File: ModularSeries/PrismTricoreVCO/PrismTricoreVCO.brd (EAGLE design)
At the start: 81 x 49 mm, 56 parts, among them IC1 LM13700_DIP, IC2 TL0X4_DIP, IC3 TL0X4_DIP, Q1 2N3906, Q2 2N3906

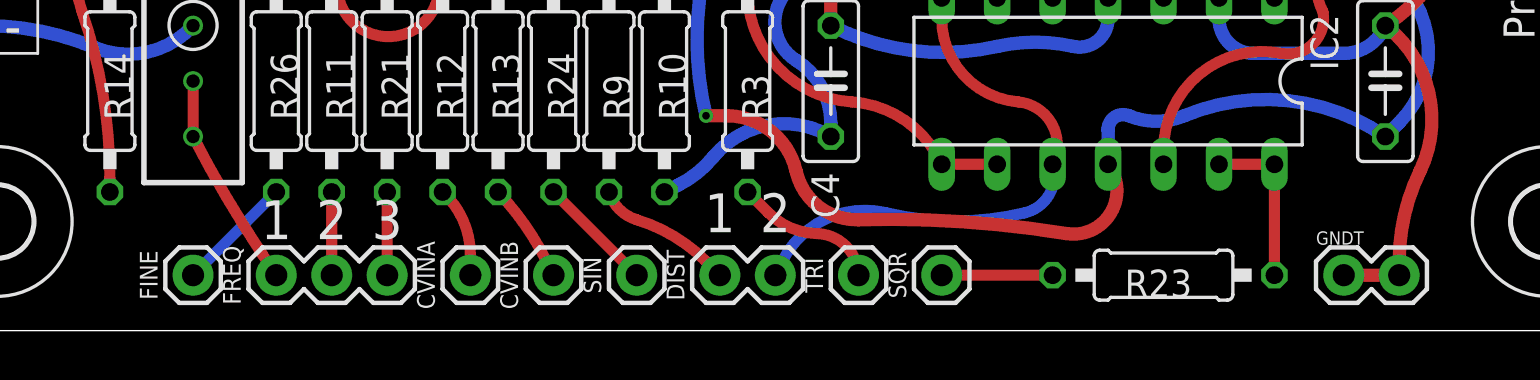
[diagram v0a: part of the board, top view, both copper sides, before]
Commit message: Updates to Prism, VCA, PSU and Prism BOM added
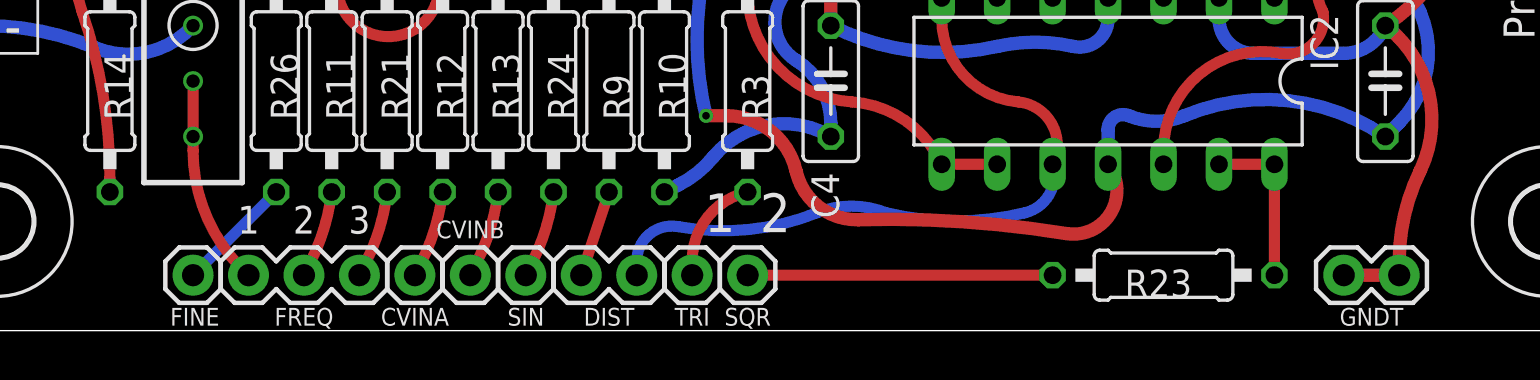
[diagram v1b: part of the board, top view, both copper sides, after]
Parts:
- moved SQR 8.89 mm to (39.4, 2.54)
- moved TRI 7.62 mm to (36.8, 2.54)
- moved DIST 6.35 mm to (31.8, 2.54)
- moved SIN 5.08 mm to (29.2, 2.54)
- moved CVINB 3.81 mm to (26.7, 2.54)
- moved CVINA 2.54 mm to (24.1, 2.54)
- moved FREQ 1.27 mm to (16.5, 2.54)
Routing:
- net N$30: track 5.08 -> 14.0 mm
- net N$2: track 54.5 -> 61.2 mm
- net N$13: track 6.40 -> 4.02 mm
- net N$29: track 6.46 -> 4.70 mm
- net N$31: track 5.39 -> 4.02 mm
- net N$28: track 4.59 -> 4.02 mm
- net N$25: track 9.95 -> 9.43 mm

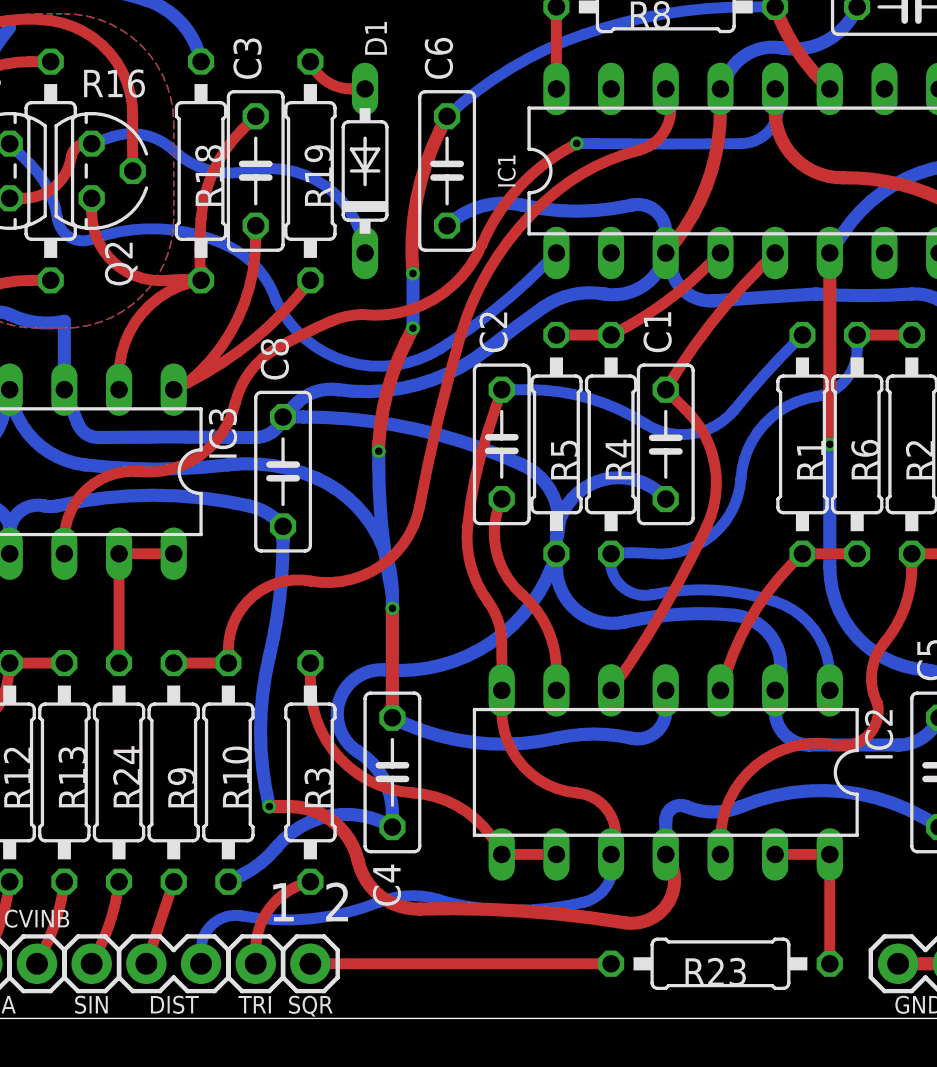
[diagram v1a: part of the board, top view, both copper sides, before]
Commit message: C2 removed from Prism
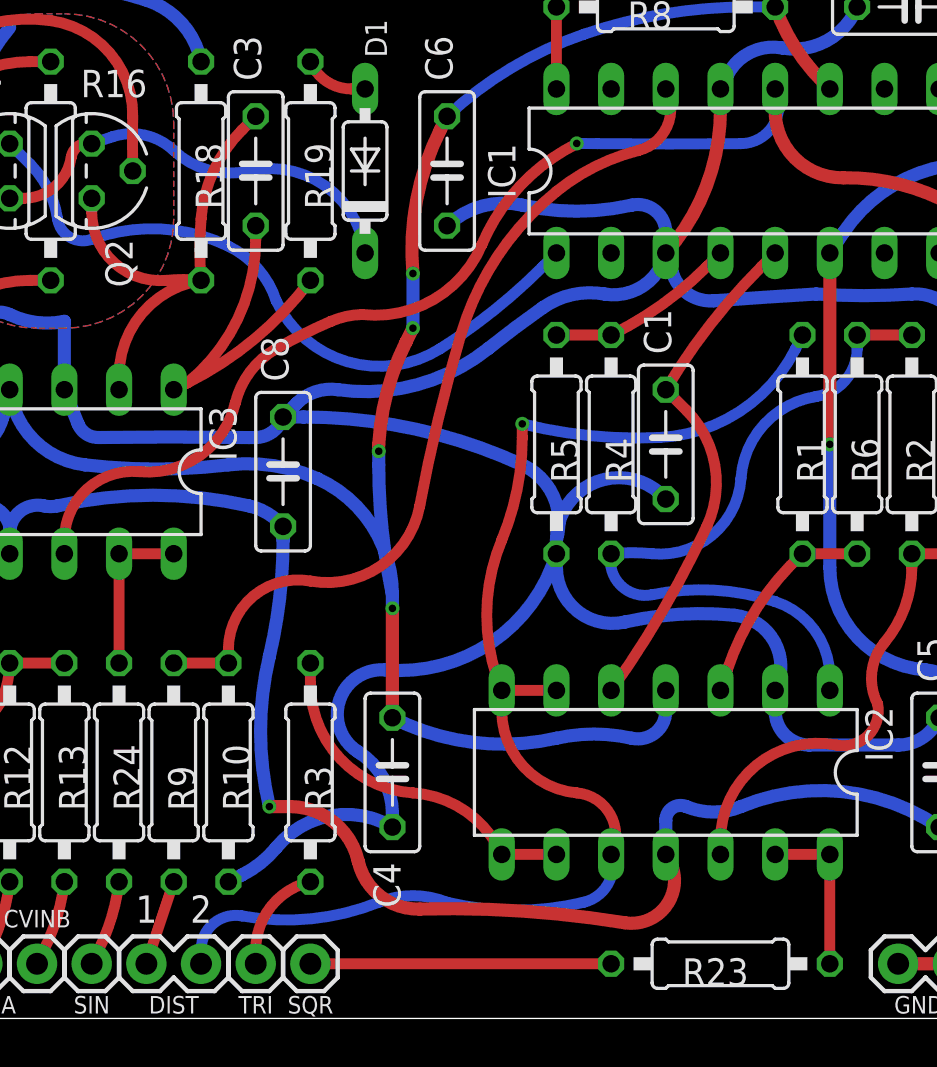
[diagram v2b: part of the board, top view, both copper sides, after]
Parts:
- removed C2: 22pF, rcl:C050-025X075
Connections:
- removed net N$2: C2.2, DIST.2, IC2.10, IC2.7, R1.2
- net N$1: now also DIST.2, IC2.10, IC2.7, R1.2; no longer C2.1
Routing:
- net N$2: track 61.2 -> 0.00 mm
- net N$1: track 9.33 -> 60.7 mm, vias 0 -> 1
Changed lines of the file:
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@@
 <text x="19.05" y="5.08" size="1.27" layer="21" font="vector" ratio="12" align="center">2</text>
 <text x="16.51" y="5.08" size="1.27" layer="21" font="vector" ratio="12" align="center">1</text>
-<text x="38.1" y="5.3975" size="1.778" layer="21" font="vector" align="center">1</text>
-<text x="40.64" y="5.3975" size="1.778" layer="21" font="vector" align="center">2</text>
+<text x="31.75" y="5.08" size="1.27" layer="21" font="vector" ratio="12" align="center">1</text>
+<text x="34.29" y="5.08" size="1.27" layer="21" font="vector" ratio="12" align="center">2</text>
 <wire x1="5" y1="49" x2="76" y2="49" width="0" layer="20"/>
 <wire x1="76" y1="49" x2="81" y2="44" width="0" layer="20" curve="-90"/>
@@
 <attribute name="VALUE" x="53.086" y="30.099" size="1.27" layer="27" ratio="10" rot="R270"/>
 </element>
-<element name="C2" library="rcl" library_urn="urn:adsk.eagle:library:334" package="C050-025X075" package3d_urn="urn:adsk.eagle:package:23637/1" value="22pF" x="48.26" y="26.67" smashed="yes" rot="R90">
-<attribute name="NAME" x="48.514" y="30.861" size="1.27" layer="25" ratio="10" rot="R90"/>
-<attribute name="POPULARITY" value="29" x="74.93" y="52.07" size="1.778" layer="27" rot="R90" display="off"/>
-<attribute name="SPICEPREFIX" value="C" x="74.93" y="52.07" size="1.778" layer="27" rot="R90" display="off"/>
-<attribute name="VALUE" x="51.054" y="23.241" size="1.27" layer="27" ratio="10" rot="R90"/>
-</element>
 <element name="C3" library="rcl" library_urn="urn:adsk.eagle:library:334" package="C050-025X075" package3d_urn="urn:adsk.eagle:package:23637/1" value="22pF" x="36.83" y="39.37" smashed="yes" rot="R90">
 <attribute name="NAME" x="37.084" y="43.561" size="1.27" layer="25" ratio="10" rot="R90"/>
@@
 </element>
 <element name="IC1" library="ElectricNoodleBox" package="DIL16" package3d_urn="urn:adsk.eagle:package:922/2" value="LM13700_DIP" x="59.69" y="39.37" smashed="yes">
-<attribute name="NAME" x="48.895" y="39.37" size="0.8128" layer="25" font="vector" ratio="20" rot="R90" align="bottom-center"/>
+<attribute name="NAME" x="48.895" y="39.37" size="1.27" layer="25" font="vector" ratio="20" rot="R90" align="bottom-center"/>
 <attribute name="VALUE" x="71.12" y="39.37" size="0.6096" layer="27" font="vector" ratio="20" rot="R90" align="bottom-center"/>
 </element>
@@
 </signal>
 <signal name="N$1">
-<contactref element="C2" pad="1"/>
 <contactref element="IC2" pad="6"/>
-<wire x1="50.8" y1="15.24" x2="50.8" y2="16.1925" width="0.508" layer="1"/>
-<wire x1="50.8" y1="16.1925" x2="49.2125" y2="19.685" width="0.508" layer="1" curve="48.88791"/>
-<wire x1="49.2125" y1="19.685" x2="48.26" y2="24.13" width="0.508" layer="1" curve="-73.586337"/>
-</signal>
-<signal name="N$2">
-<contactref element="C2" pad="2"/>
 <contactref element="R1" pad="2"/>
 <contactref element="DIST" pad="2"/>
 <contactref element="IC2" pad="10"/>
 <contactref element="IC2" pad="7"/>
-<wire x1="48.26" y1="29.21" x2="47.625" y2="27.305" width="0.508" layer="1"/>
-<wire x1="47.625" y1="27.305" x2="46.6725" y2="22.86" width="0.508" layer="1" curve="12.680383"/>
-<wire x1="46.6725" y1="22.86" x2="47.625" y2="19.3675" width="0.508" layer="1" curve="42.01933"/>
-<wire x1="47.625" y1="19.3675" x2="48.26" y2="17.4625" width="0.508" layer="1" curve="-35.659716"/>
-<wire x1="48.26" y1="17.4625" x2="48.26" y2="15.24" width="0.508" layer="1" curve="-1.210224"/>
-<wire x1="48.26" y1="29.21" x2="49.53" y2="29.21" width="0.508" layer="16"/>
-<wire x1="49.53" y1="29.21" x2="54.9275" y2="27.6225" width="0.508" layer="16" curve="-32.779081"/>
-<wire x1="54.9275" y1="27.6225" x2="59.055" y2="28.2575" width="0.508" layer="16" curve="83.050492"/>
 <wire x1="48.26" y1="15.24" x2="48.26" y2="14.2875" width="0.508" layer="1"/>
 <wire x1="48.26" y1="14.2875" x2="51.7525" y2="10.4775" width="0.508" layer="1" curve="85.020903"/>
@@
 <wire x1="45.72" y1="5.3975" x2="52.07" y2="5.3975" width="0.508" layer="16" curve="26.802372"/>
 <wire x1="52.07" y1="5.3975" x2="53.34" y2="7.62" width="0.508" layer="16" curve="93.707892"/>
-<wire x1="62.23" y1="31.75" x2="61.9125" y2="31.4325" width="0.508" layer="16"/>
-<wire x1="61.9125" y1="31.4325" x2="59.055" y2="28.2575" width="0.508" layer="16" curve="6.025575"/>
 <wire x1="34.29" y1="2.54" x2="34.29" y2="3.175" width="0.508" layer="16"/>
 <wire x1="34.29" y1="3.175" x2="36.195" y2="4.7625" width="0.508" layer="16" curve="-100.388821"/>
 <wire x1="36.195" y1="4.7625" x2="42.545" y2="5.3975" width="0.508" layer="16" curve="32.198904"/>
 <wire x1="42.545" y1="5.3975" x2="45.72" y2="5.3975" width="0.508" layer="16" curve="-43.620125"/>
+<wire x1="50.8" y1="15.24" x2="48.26" y2="15.24" width="0.508" layer="1"/>
+<wire x1="62.23" y1="31.75" x2="61.9125" y2="31.115" width="0.508" layer="16"/>
+<wire x1="61.9125" y1="31.115" x2="55.5625" y2="26.9875" width="0.508" layer="16" curve="-60.822161"/>
+<wire x1="55.5625" y1="26.9875" x2="49.2125" y2="27.6225" width="0.508" layer="16" curve="-16.64677"/>
+<via x="49.2125" y="27.6225" extent="1-16" drill="0.35"/>
+<wire x1="49.2125" y1="27.6225" x2="49.2125" y2="26.9875" width="0.508" layer="1"/>
+<wire x1="49.2125" y1="26.9875" x2="48.26" y2="22.225" width="0.508" layer="1" curve="-22.619865"/>
+<wire x1="48.26" y1="22.225" x2="48.26" y2="15.24" width="0.508" layer="1" curve="45.239684"/>
 </signal>
 <signal name="N$3">

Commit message: Library updated, variants consolidated
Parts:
- IC1: value LM13700_DIP -> (none)
- IC2, IC3: value TL0X4_DIP -> (none)
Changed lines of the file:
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@@
 <attribute name="VALUE" x="30.48" y="0.508" size="0.6096" layer="27" font="vector" ratio="20"/>
 </element>
-<element name="IC1" library="ElectricNoodleBox" package="DIL16" package3d_urn="urn:adsk.eagle:package:922/2" value="LM13700_DIP" x="59.69" y="39.37" smashed="yes">
+<element name="IC1" library="ElectricNoodleBox" package="DIL16" package3d_urn="urn:adsk.eagle:package:922/2" value="" x="59.69" y="39.37" smashed="yes">
 <attribute name="NAME" x="48.895" y="39.37" size="1.27" layer="25" font="vector" ratio="20" rot="R90" align="bottom-center"/>
 <attribute name="VALUE" x="71.12" y="39.37" size="0.6096" layer="27" font="vector" ratio="20" rot="R90" align="bottom-center"/>
 </element>
-<element name="IC2" library="ElectricNoodleBox" package="DIL14" package3d_urn="urn:adsk.eagle:package:16407/2" value="TL0X4_DIP" x="55.88" y="11.43" smashed="yes" rot="R180">
+<element name="IC2" library="ElectricNoodleBox" package="DIL14" package3d_urn="urn:adsk.eagle:package:16407/2" value="" x="55.88" y="11.43" smashed="yes" rot="R180">
 <attribute name="NAME" x="65.151" y="14.478" size="1.27" layer="25" ratio="10" rot="R270"/>
 <attribute name="VALUE" x="62.611" y="12.065" size="1.27" layer="27" ratio="10" rot="R180"/>
 </element>
-<element name="IC3" library="ElectricNoodleBox" package="DIL14" package3d_urn="urn:adsk.eagle:package:16407/2" value="TL0X4_DIP" x="25.4" y="25.4" smashed="yes" rot="R180">
+<element name="IC3" library="ElectricNoodleBox" package="DIL14" package3d_urn="urn:adsk.eagle:package:16407/2" value="" x="25.4" y="25.4" smashed="yes" rot="R180">
 <attribute name="NAME" x="34.671" y="28.448" size="1.27" layer="25" ratio="10" rot="R270"/>
 <attribute name="VALUE" x="32.131" y="26.035" size="1.27" layer="27" ratio="10" rot="R180"/>

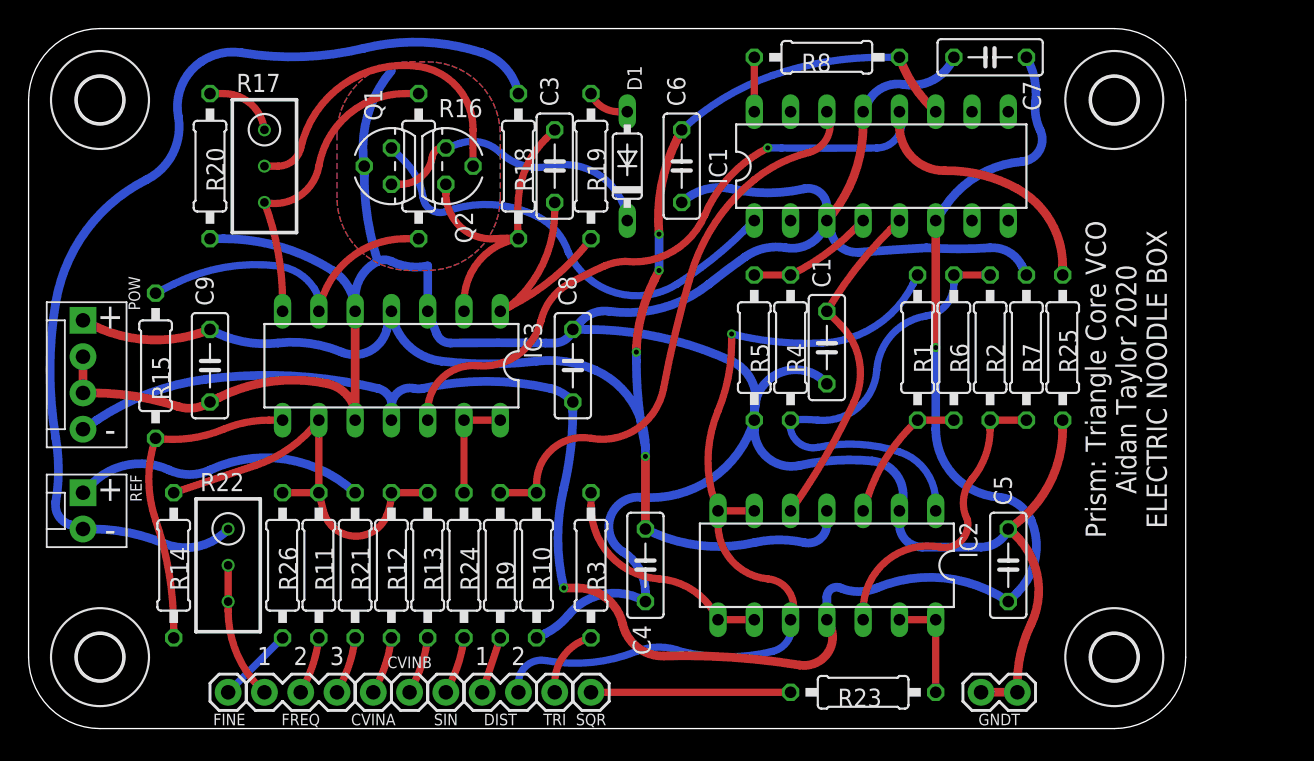
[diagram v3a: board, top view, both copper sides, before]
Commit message: Power header updated on most PCBs. Knives layout added
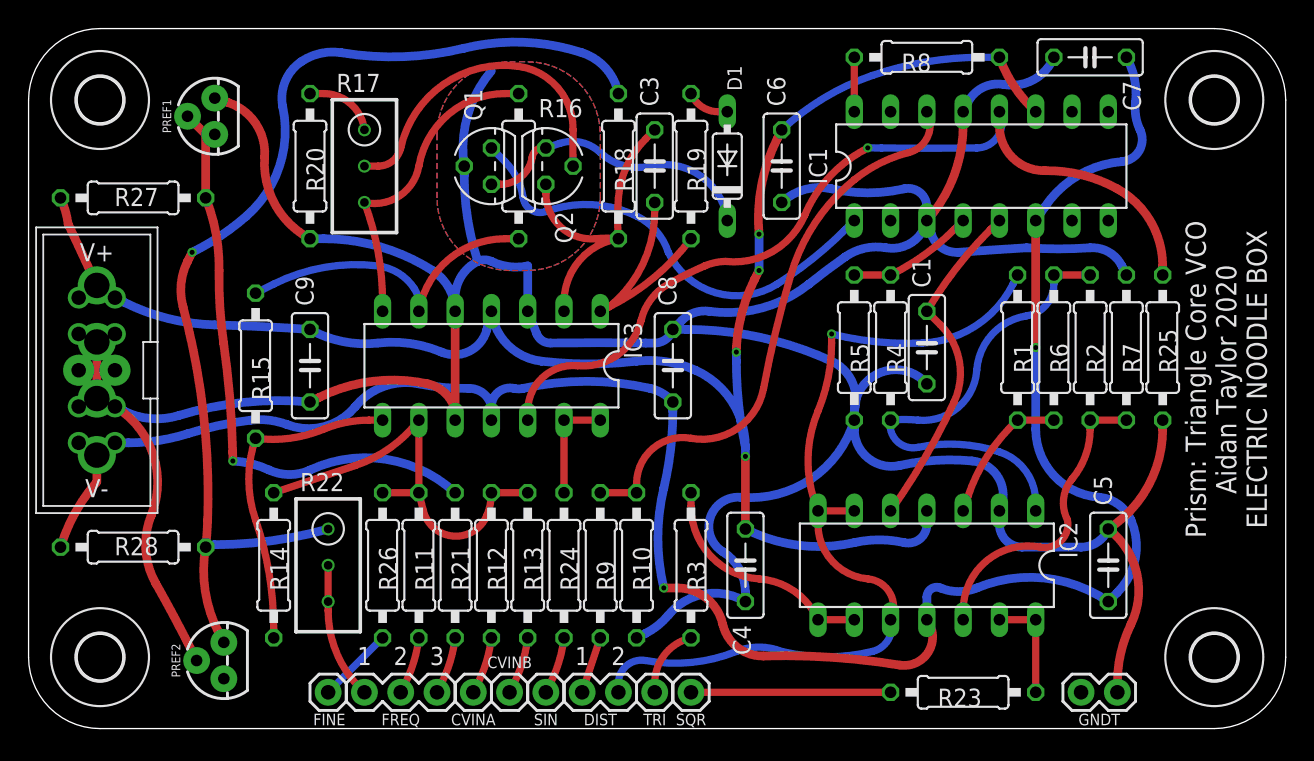
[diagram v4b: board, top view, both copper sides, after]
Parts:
- removed POW: 4XMOLEX, ElectricNoodleBox:MOLEX-1X4
- removed REF: 2XMOLEX, ElectricNoodleBox:MOLEX-1X2
- added PREF1, PREF2: (no value), ElectricNoodleBox:TO-92
- added R27, R28: 10K, rcl:0207/10
- added WP1: COMBO_SUPPLY_HEADER, ElectricNoodleBox:COMBINED_POWER
- moved R1 7.00 mm to (69.2, 26.7)
- moved C1 7.00 mm to (62.9, 26.7)
- moved C3 7.00 mm to (43.8, 39.4)
- moved C4 7.00 mm to (50.2, 11.4)
- moved C5 7.00 mm to (75.6, 11.4)
- moved C6 7.00 mm to (52.7, 39.4)
- moved C7 7.00 mm to (74.3, 47.0)
- moved C8 7.00 mm to (45.1, 25.4)
- moved C9 7.00 mm to (19.7, 25.4)
- moved CVINA 7.00 mm to (31.1, 2.54)
- moved CVINB 7.00 mm to (33.7, 2.54)
- moved D1 7.00 mm to (48.9, 39.4)
- moved DIST 7.00 mm to (38.8, 2.54)
- moved FREQ 7.00 mm to (23.5, 2.54)
- moved GNDT 7.00 mm to (73.7, 2.54)
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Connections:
- net +10VREF: now also PREF1.2, R27.1; no longer REF.1
- net +12V: now also R27.2, WP1.V+1, WP1.V+2, WP1.V+3; no longer POW.1
- net -10VREF: now also PREF2.3, R28.1; no longer REF.2
- net -12V: now also R28.2, WP1.V-1, WP1.V-2, WP1.V-3; no longer POW.4
- net AGND: now also PREF1.3, PREF2.2, WP1.GND1, WP1.GND2, WP1.GND3, WP1.GND4, WP1.GND5, WP1.GND6, WP1.GND7, WP1.GND8; no longer POW.2, POW.3
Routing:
- net AGND: track 234.4 -> 278.8 mm
- net +10VREF: track 19.5 -> 40.5 mm, vias 0 -> 1
- net -12V: track 132.1 -> 147.0 mm
- net +12V: track 108.9 -> 123.6 mm
- net -10VREF: track 70.5 -> 75.9 mm, vias 0 -> 1
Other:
- board size 81 x 49 mm -> 88 x 49 mm
- board text removed: "+"
- board text removed: "-"
